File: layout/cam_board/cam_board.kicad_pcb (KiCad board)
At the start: 4 copper layers, 60 x 45 mm, 82 parts, among them J1 Stick conn, J2 LCD conn, J3 Conn_01x05_Pin, J4 USB Connector, J5 BATT_CONNECTOR, M1 MountingHole_2.1mm, M2 MountingHole_2.1mm, SW1 BOOT0, SW2 USER, SW3 NRST, SW4 ON/OFF, U1 W25Q128JVS, U2 STM32F401CCUx, U3 AP2112K-3.3, U4 MCP73871-1AA, U5 USBLC6-2SC6, Y1 SC32S-7PF20PPM, Y2 ECS-80-18-23B-JTN-TR

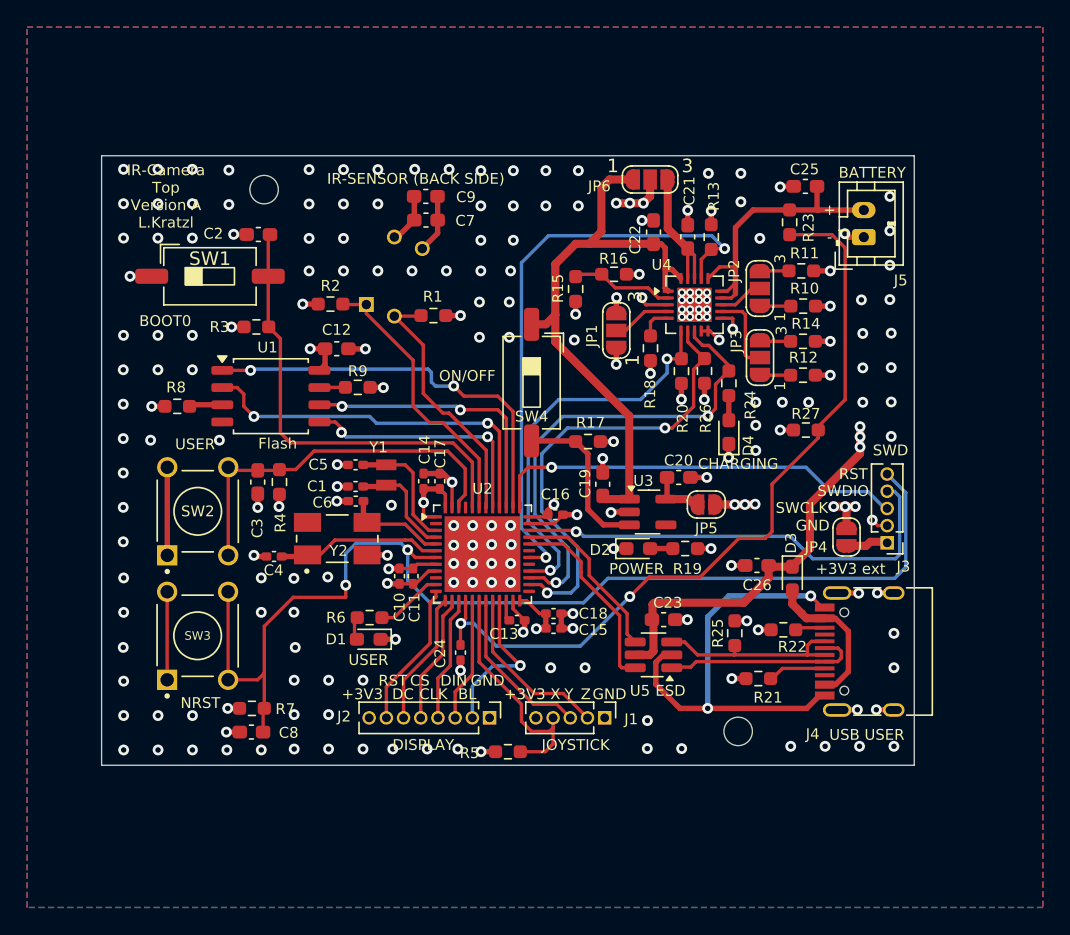
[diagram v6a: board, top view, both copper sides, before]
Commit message: Changed foot print to 0603 for allk capacitors Changed footprints for connectors to 2.54 mm Fixed footprint of 32 MHz crystal / Y1 Change slider footprint from SMD to THT Remove USB pull up 1k5 Introduce Keep-Out zone
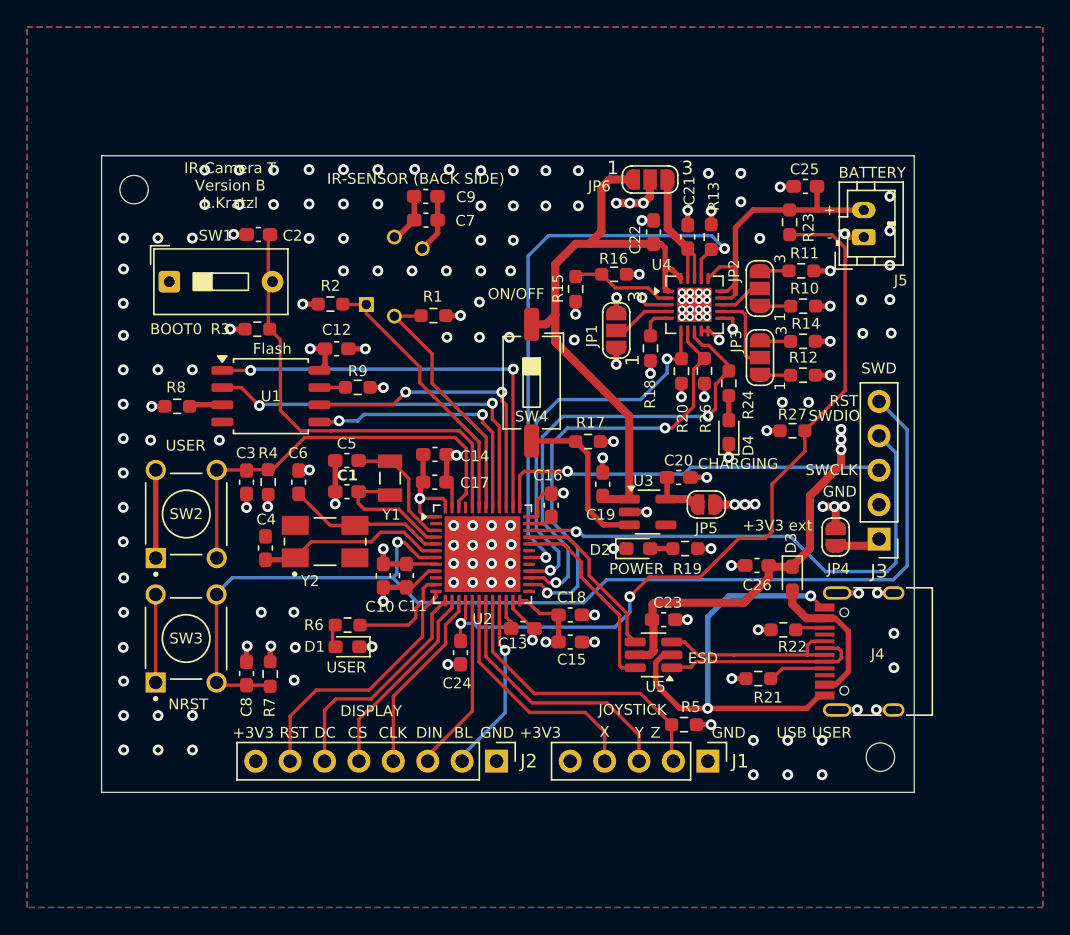
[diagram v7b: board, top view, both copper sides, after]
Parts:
- removed R25: 1k5, Resistor_SMD:R_0603_1608Metric_Pad0.98x0.95mm_HandSolder
- C1, C10, C11, C13, C14, C15, C16, C17, C18, C24, C4, C5, C6: footprint Capacitor_SMD:C_0402_1005Metric_Pad0.74x0.62mm_HandSolder -> Capacitor_SMD:C_0603_1608Metric_Pad1.08x0.95mm_HandSolder
- C9: value 10u -> 10uF
- J1, J3: footprint Connector_PinHeader_1.27mm:PinHeader_1x05_P1.27mm_Vertical -> Connector_PinHeader_2.54mm:PinHeader_1x05_P2.54mm_Vertical
- J2: footprint Connector_PinHeader_1.27mm:PinHeader_1x08_P1.27mm_Vertical -> Connector_PinHeader_2.54mm:PinHeader_1x08_P2.54mm_Vertical
- SW1: footprint Button_Switch_SMD:SW_DIP_SPSTx01_Slide_6.7x4.1mm_W8.61mm_P2.54mm_LowProfile -> Button_Switch_THT:SW_DIP_SPSTx01_Slide_9.78x4.72mm_W7.62mm_P2.54mm
- Y1: footprint A_Custom:XTAL_CM8V-T1A-32.768KHZ-6PF-20PPM-TA-QC -> A_Custom:XTAL_CTS3-32.768-12.5-20-CT
- moved R5 13.2 mm to (111.0, 74.0), turned to 180 degrees
- moved M2 10.7 mm to (125.5, 76.4)
- moved M1 9.60 mm to (70.4, 34.5)
- moved J1 8.26 mm to (112.8, 76.7)
- moved C6 4.44 mm to (82.5, 56.1), turned to -90 degrees
- moved C8 4.34 mm to (78.7, 70.2), turned to -90 degrees
- moved J2 3.24 mm to (97.2, 76.7)
- moved SW1 3.03 mm to (73.0, 41.3)
- moved R7 2.87 mm to (80.5, 70.3), turned to -90 degrees
- moved C14 2.15 mm to (92.6, 54.0), turned to 180 degrees
- moved R6 1.72 mm to (86.2, 66.7)
- moved D1 1.67 mm to (86.2, 68.2)
- moved C15 1.59 mm to (102.6, 67.9)
- moved C18 1.24 mm to (102.6, 65.9)
- moved C10 1.20 mm to (88.8, 63.0)
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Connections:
- R5 pad 2: STICK_X -> STICK_Z
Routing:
- net STICK_Z: track 12.8 -> 22.0 mm
- net RST: track 10.9 -> 19.3 mm
- net DC: track 9.93 -> 17.1 mm
- net STICK_Y: track 12.2 -> 19.4 mm
- net +3V3: track 45.1 -> 50.8 mm, vias 20 -> 18
- net CS: track 9.62 -> 14.8 mm
- net SWDIO: track 33.7 -> 38.5 mm
- net CLK: track 9.29 -> 13.9 mm
- net DIN: track 9.18 -> 12.8 mm
- net OSC_IN: track 7.42 -> 10.9 mm
- net USER_LED: track 5.00 -> 8.43 mm
- net USRBUTTON: track 28.3 -> 30.9 mm
- net OSC_OUT: track 11.4 -> 14.0 mm
- net OSC32_OUT: track 8.12 -> 10.2 mm
- net GND: track 75.3 -> 73.3 mm, vias 194 -> 159
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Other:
- board size 60 x 45 mm -> 60 x 47 mm
- board text added: "IR-Camera B Version A L.Kratzl"
- board text added: "IR-Camera T Version B L.Kratzl"
- board text removed: "IR-Camera Bottom Version A L.Kratzl"
- board text removed: "IR-Camera Top Version A L.Kratzl"

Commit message: Update
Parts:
- moved D1 15.9 mm to (73.1, 77.3)
- moved R6 15.9 mm to (73.2, 75.7)
- moved C6 13.0 mm to (84.3, 69.0), turned to 0 degrees
- moved C4 4.32 mm to (84.3, 60.0), turned to 180 degrees
- moved Y2 3.97 mm to (84.3, 64.5), turned to -90 degrees
- moved C8 1.74 mm to (77.0, 70.3)
- moved R7 1.74 mm to (78.7, 70.3)
- moved C3 1.74 mm to (77.0, 56.2)
- moved R4 1.74 mm to (78.6, 56.2)
- moved SW3 1.74 mm to (72.5, 67.7)
- moved SW2 1.74 mm to (72.5, 58.5)
- moved C5 1.56 mm to (84.6, 54.3)
- moved C1 1.56 mm to (84.6, 56.6)
- moved Y1 1.56 mm to (87.8, 55.6)
- moved R27 1.38 mm to (117.6, 52.4)
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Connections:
- C4 pad 2: OSC_OUT -> OSC_IN
- C6 pad 2: OSC_IN -> OSC_OUT
- Y2 pad 1: OSC_OUT -> OSC_IN
- Y2 pad 3: OSC_IN -> OSC_OUT
- Y2 pad 4: (no net) -> GND
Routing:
- net USER_LED: track 8.43 -> 25.0 mm
- net GND: track 73.3 -> 79.8 mm, vias 159 -> 141
- net OSC_IN: track 10.9 -> 13.1 mm
- net OSC_OUT: track 14.0 -> 15.8 mm
- net USRBUTTON: track 30.9 -> 32.6 mm
- net OSC32_IN: track 8.84 -> 10.6 mm
- net NRST: track 83.1 -> 84.8 mm
- net BATTLVL: track 57.8 -> 59.2 mm
- net OSC32_OUT: track 10.2 -> 8.84 mm
- net VIN: track 43.4 -> 42.2 mm
